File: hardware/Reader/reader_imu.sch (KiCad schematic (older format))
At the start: 6 parts

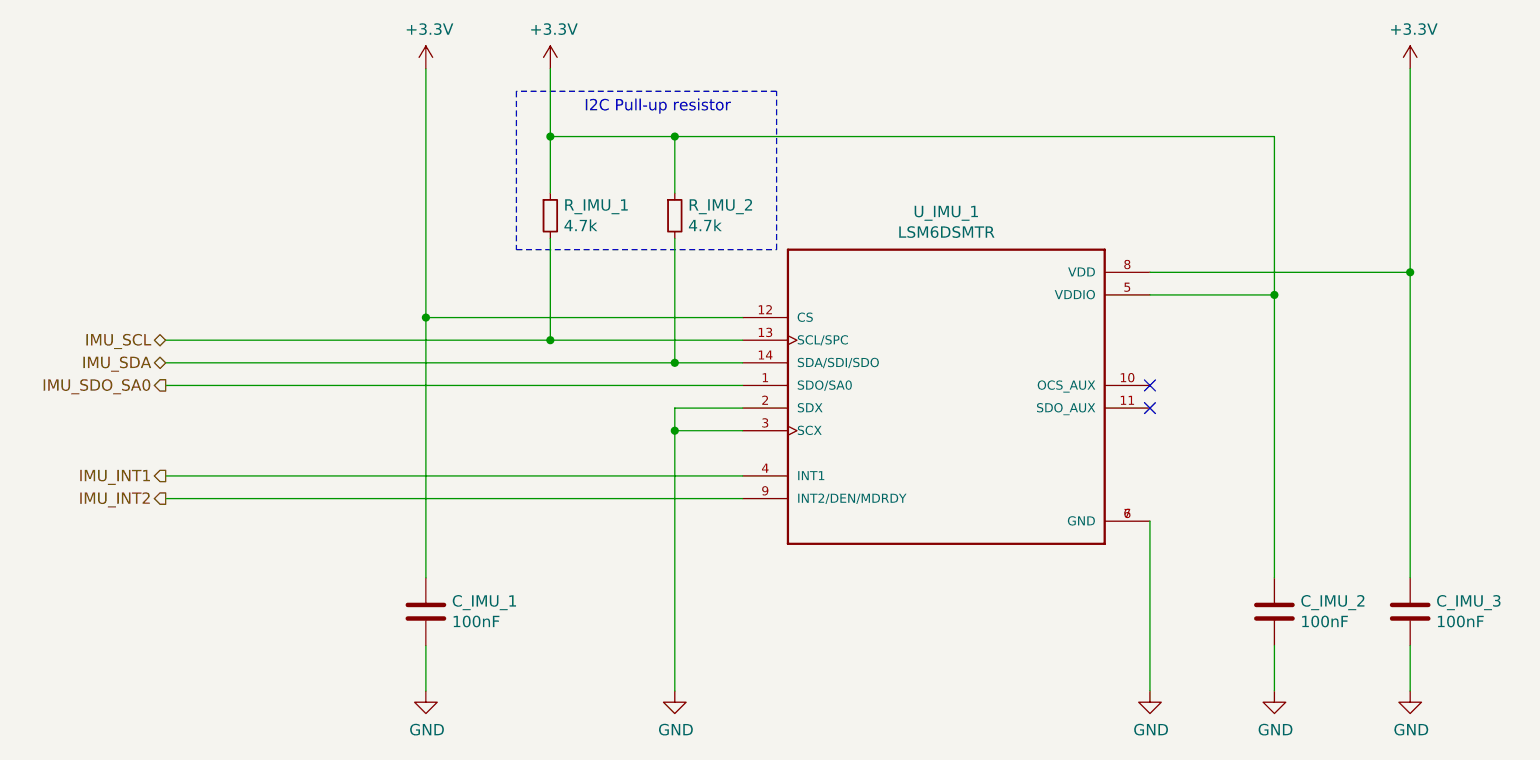
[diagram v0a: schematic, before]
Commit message: Updated schematic and gerber to v0.0.05. Added ESP32. Removed MS CAN and SW CAN Transceivers. Added silkscreen text to header pins. Improved readability
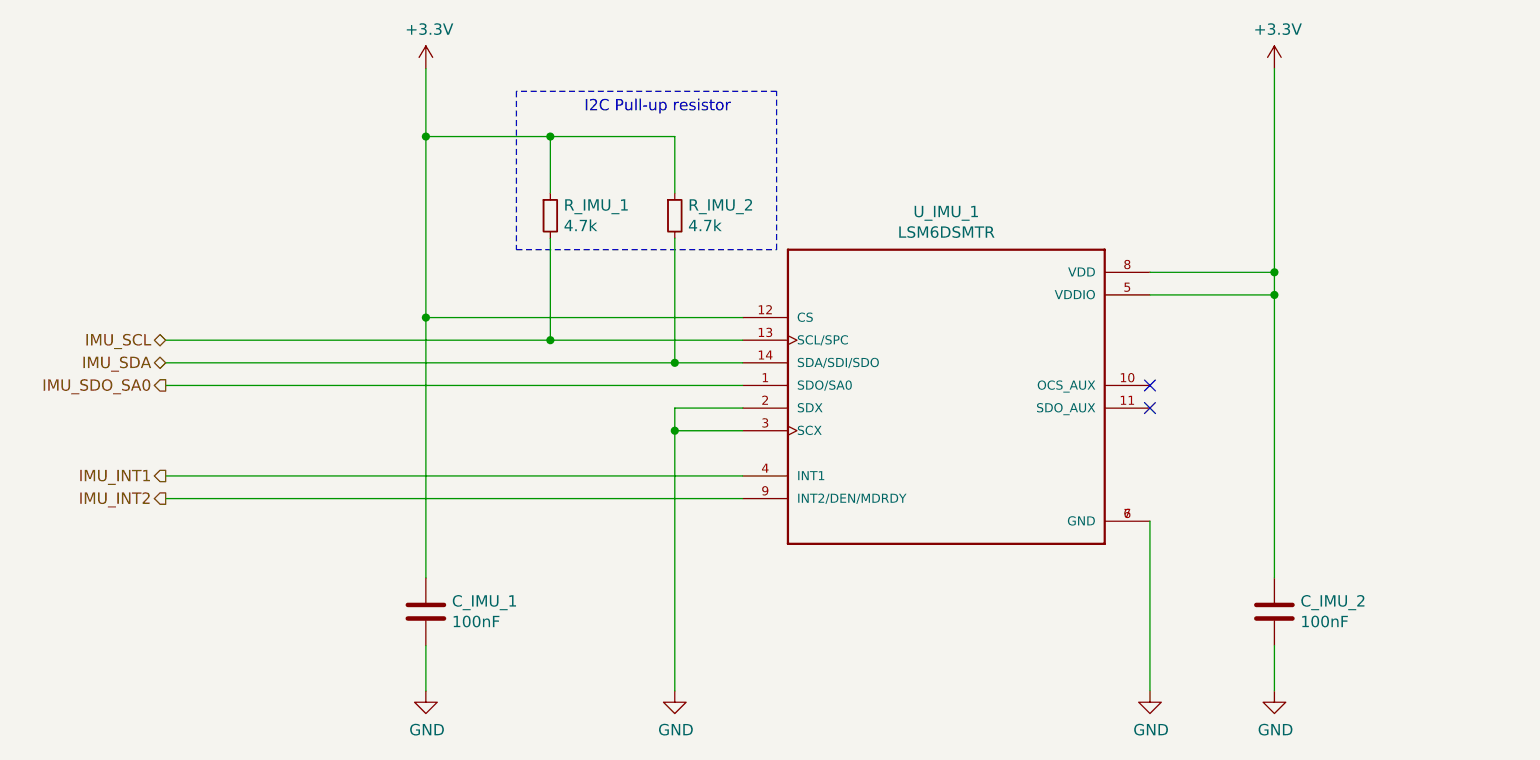
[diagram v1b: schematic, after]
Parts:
- removed C_IMU_3: 100nF, footprints:CAPC1608X90N, symbol Device:C
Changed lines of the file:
@@
 $Descr A4 11693 8268
 encoding utf-8
-Sheet 9 17
+Sheet 11 17
 Title "CANnect Reader | IMU"
-Date "2020-11-27"
+Date "2020-11-29"
 Rev "0.0.05"
 Comp "CANtech"
@@
 Text HLabel 3300 3950 0    50   Output ~ 0
 IMU_INT1
-Text HLabel 3300 3550 0    50   Output ~ 0
-IMU_SDO_SA0
 Text HLabel 3300 4050 0    50   Output ~ 0
 IMU_INT2
 Wire Wire Line
 	3300 3450 5550 3450
-Wire Wire Line
-	5850 3550 3300 3550
 Wire Wire Line
 	5850 3950 3300 3950
@@
 Wire Wire Line
 	5550 2700 5550 2450
-Connection ~ 5550 2450
 Wire Wire Line
 	5550 2450 5000 2450
 Wire Wire Line
-	8200 3150 8200 2450
+	8200 3150 8200 3050
 Wire Wire Line
 	7650 3150 8200 3150
-Wire Wire Line
-	5550 2450 8200 2450
 Wire Wire Line
 	8200 4400 8200 3150
@@
 F 3 "" H 4450 4900 50  0001 C CNN
 	1    4450 4900
-	1    0    0    -1
-$EndComp
-$Comp
-L power:GND #PWR?
-U 1 1 5FC30E64
-P 8800 4900
-AR Path="/5FC30E64" Ref="#PWR?"  Part="1"
-AR Path="/5F988046/5FC30E64" Ref="#PWR?"  Part="1"
-AR Path="/5FC2797A/5FC30E64" Ref="#PWR0145"  Part="1"
-F 0 "#PWR0145" H 8800 4650 50  0001 C CNN
-F 1 "GND" H 8805 4727 50  0000 C CNN
-F 2 "" H 8800 4900 50  0001 C CNN
-F 3 "" H 8800 4900 50  0001 C CNN
-	1    8800 4900
 	1    0    0    -1
 $EndComp
@@
 	1    0    0    -1
 $EndComp
-$Comp
-L Device:C C_IMU_3
-U 1 1 5FC32983
-P 8800 4550
-F 0 "C_IMU_3" H 8915 4596 50  0000 L CNN
-F 1 "100nF" H 8915 4505 50  0000 L CNN
-F 2 "footprints:CAPC1608X90N" H 8838 4400 50  0001 C CNN
-F 3 "https://product.tdk.com/info/en/catalog/datasheets/mlcc_commercial_midvoltage_en.pdf" H 8800 4550 50  0001 C CNN
-F 4 "TDK Corporation" H 8800 4550 50  0001 C CNN "Manufacturer"
-F 5 "C1608X7R2A103K080AA" H 8800 4550 50  0001 C CNN "Part Name"
-F 6 "DigiKey Canada" H 8800 4550 50  0001 C CNN "Vendor"
-F 7 "445-1304-1-ND" H 8800 4550 50  0001 C CNN "digikeypn"
-	1    8800 4550
-	1    0    0    -1
-$EndComp
 Wire Wire Line
 	8200 4700 8200 4900
-Wire Wire Line
-	8800 4900 8800 4700
 $Comp
 L power:GND #PWR?
@@
 	7650 4150 7650 4900
 Wire Wire Line
-	7650 3050 8800 3050
-Wire Wire Line
-	8800 3050 8800 4400
-Wire Wire Line
-	8800 2150 8800 3050
-Connection ~ 8800 3050
-Wire Wire Line
 	4450 3250 5850 3250
 Wire Wire Line
@@
 	5550 3750 5550 4900
 Wire Wire Line
-	4450 2150 4450 3250
-Wire Wire Line
-	5000 2150 5000 2450
+	4450 2150 4450 2450
 $Comp
 L power:+3.3V #PWR0148
@@
 $EndComp
 $Comp
-L power:+3.3V #PWR0149
-U 1 1 5FE5FC30
-P 5000 2150
-F 0 "#PWR0149" H 5000 2000 50  0001 C CNN
-F 1 "+3.3V" H 5015 2323 50  0000 C CNN
-F 2 "" H 5000 2150 50  0001 C CNN
-F 3 "" H 5000 2150 50  0001 C CNN
-	1    5000 2150
-	1    0    0    -1
-$EndComp
-$Comp
 L power:+3.3V #PWR0150
 U 1 1 5FE5FDC5
-P 8800 2150
-F 0 "#PWR0150" H 8800 2000 50  0001 C CNN
-F 1 "+3.3V" H 8815 2323 50  0000 C CNN
-F 2 "" H 8800 2150 50  0001 C CNN
-F 3 "" H 8800 2150 50  0001 C CNN
-	1    8800 2150
-	1    0    0    -1
-$EndComp
+P 8200 2150
+F 0 "#PWR0150" H 8200 2000 50  0001 C CNN
+F 1 "+3.3V" H 8215 2323 50  0000 C CNN
+F 2 "" H 8200 2150 50  0001 C CNN
+F 3 "" H 8200 2150 50  0001 C CNN
+	1    8200 2150
+	1    0    0    -1
+$EndComp
+Wire Wire Line
+	7650 3050 8200 3050
+Wire Wire Line
+	8200 2150 8200 3050
+Connection ~ 8200 3050
+Wire Wire Line
+	5000 2450 4450 2450
+Connection ~ 4450 2450
+Wire Wire Line
+	4450 2450 4450 3250
+Text HLabel 3300 3550 0    50   Output ~ 0
+IMU_SDO_SA0
+Wire Wire Line
+	5850 3550 3300 3550
 $EndSCHEMATC
